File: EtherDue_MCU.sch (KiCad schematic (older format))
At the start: 30 parts, among them IC201 ATSAM3X8E, SW201 ERASE, SW202 RESET, U202 FDN340P, U203 LMV358IDGKR, X201 TXC 7A 12MHz 18pF, X202 ABS07L 32.768kHz

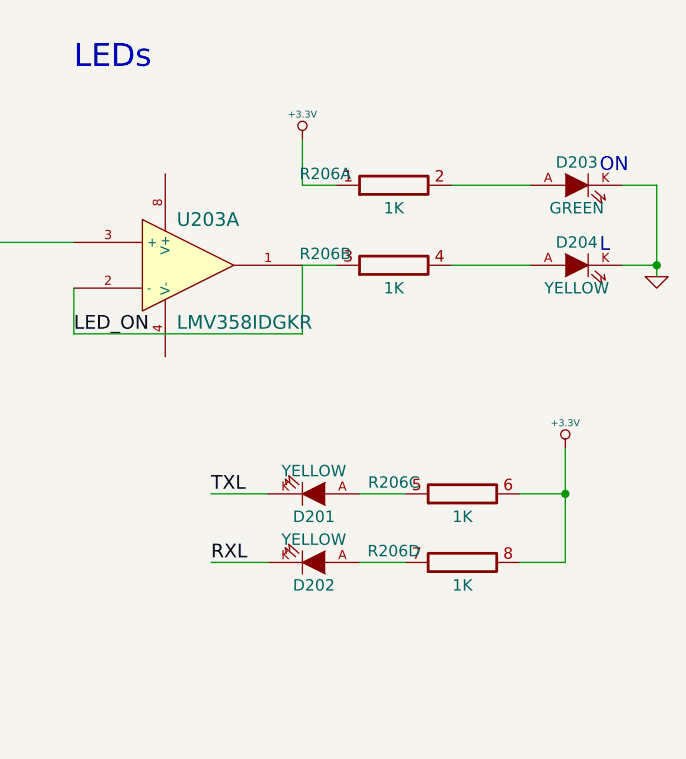
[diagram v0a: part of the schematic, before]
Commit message: Pre-autorouter hand routed traces
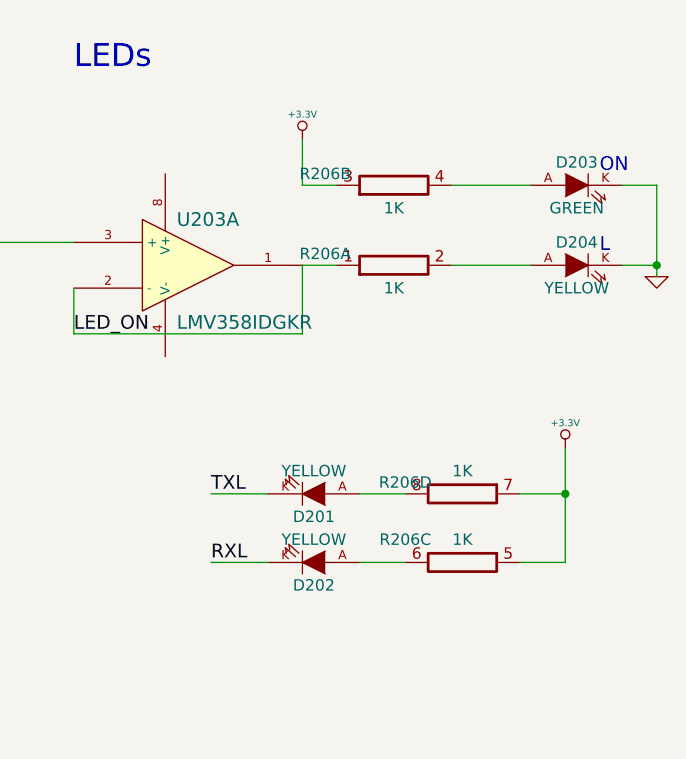
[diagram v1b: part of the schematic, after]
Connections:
- net +3.3V: now also R206.3 (7), R206.5 (7), R206.7; no longer R206.1 (7), R206.6 (8), R206.8
- net LED_ON: now also R206.1 (7); no longer R206.3 (7)
- net at R206.2 (8): now also D204.A; no longer D203.A
- net at R206.4 (8): now also D203.A; no longer D204.A
- net at D202.A: now also R206.6 (8); no longer R206.7
- net at D201.A: now also R206.8; no longer R206.5 (7)
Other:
- moved on the sheet: R206A, R206B, R206C, R206D
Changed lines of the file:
@@
-EESchema Schematic File Version 2  date Thu 06 Jun 2013 17:31:40 EST
+EESchema Schematic File Version 2  date Wed 19 Jun 2013 10:44:48 EST
 LIBS:freetronics_kicad_sch_lib
 LIBS:power
@@
 Sheet 2 6
 Title ""
-Date "6 jun 2013"
+Date "19 jun 2013"
 Rev ""
 Comp ""
@@
 L RES_PACK4_IND R206
 U 3 1 515CBE59
+P 14450 6800
+F 0 "R206" H 14700 6700 50  0000 C CNN
+F 1 "1K" H 14450 6700 50  0000 C CNN
+F 2 "" H 14450 6800 60  0001 C CNN
+F 3 "" H 14450 6800 60  0001 C CNN
+	3    14450 6800
+	-1   0    0    1
+$EndComp
+$Comp
+L RES_PACK4_IND R206
+U 4 1 515CBE58
 P 14450 6500
-F 0 "R206" H 14150 6550 50  0000 C CNN
+F 0 "R206" H 14700 6450 50  0000 C CNN
 F 1 "1K" H 14450 6400 50  0000 C CNN
 F 2 "" H 14450 6500 60  0001 C CNN
 F 3 "" H 14450 6500 60  0001 C CNN
-	3    14450 6500
-	1    0    0    -1
-$EndComp
-$Comp
-L RES_PACK4_IND R206
-U 4 1 515CBE58
-P 14450 6800
-F 0 "R206" H 14150 6850 50  0000 C CNN
-F 1 "1K" H 14450 6700 50  0000 C CNN
-F 2 "" H 14450 6800 60  0001 C CNN
-F 3 "" H 14450 6800 60  0001 C CNN
-	4    14450 6800
-	1    0    0    -1
+	4    14450 6500
+	-1   0    0    1
 $EndComp
 Text Label 13350 6800 0    60   ~ 0
@@
 L RES_PACK4_IND R206
 U 2 1 515CBD03
+P 14150 5150
+F 0 "R206" H 13850 5200 50  0000 C CNN
+F 1 "1K" H 14150 5050 50  0000 C CNN
+F 2 "" H 14150 5150 60  0001 C CNN
+F 3 "" H 14150 5150 60  0001 C CNN
+	2    14150 5150
+	1    0    0    -1
+$EndComp
+Text Notes 15050 5450 0    60   ~ 0
+L
+Text Notes 15050 5100 0    60   ~ 0
+ON
+$Comp
+L RES_PACK4_IND R206
+U 1 1 515CBD02
 P 14150 5500
 F 0 "R206" H 13850 5550 50  0000 C CNN
@@
 F 2 "" H 14150 5500 60  0001 C CNN
 F 3 "" H 14150 5500 60  0001 C CNN
-	2    14150 5500
-	1    0    0    -1
-$EndComp
-Text Notes 15050 5450 0    60   ~ 0
-L
-Text Notes 15050 5100 0    60   ~ 0
-ON
-$Comp
-L RES_PACK4_IND R206
-U 1 1 515CBD02
-P 14150 5150
-F 0 "R206" H 13850 5200 50  0000 C CNN
-F 1 "1K" H 14150 5050 50  0000 C CNN
-F 2 "" H 14150 5150 60  0001 C CNN
-F 3 "" H 14150 5150 60  0001 C CNN
-	1    14150 5150
-	1    0    0    -1
-$EndComp
+	1    14150 5500
+	1    0    0    -1
+$EndComp

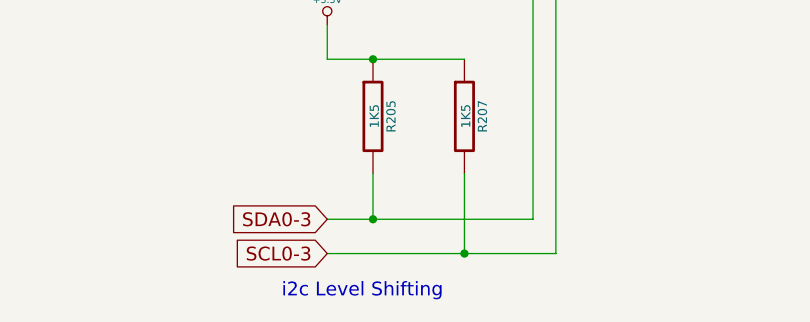
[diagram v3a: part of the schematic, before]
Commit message: Add 24AA025E48 EEPROM w/ unique MAC address
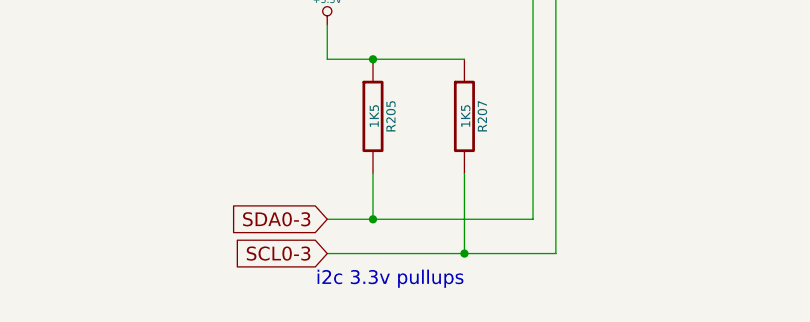
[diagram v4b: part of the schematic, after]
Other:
- note added: "i2c 3.3v pullups"
- note removed: "i2c Level Shifting"
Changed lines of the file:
@@
-EESchema Schematic File Version 2  date Fri 28 Jun 2013 16:34:50 EST
+EESchema Schematic File Version 2  date Thu 04 Jul 2013 10:55:52 EST
 LIBS:freetronics_kicad_sch_lib
 LIBS:power
@@
 $Descr A3 16535 11693
 encoding utf-8
-Sheet 2 6
+Sheet 2 7
 Title ""
-Date "27 jun 2013"
+Date "4 jul 2013"
 Rev ""
 Comp ""
@@
 Wire Wire Line
 	7600 10600 7600 8450
-Text Notes 6500 10950 0    60   ~ 0
-i2c Level Shifting
+Text Notes 6650 10900 0    60   ~ 0
+i2c 3.3v pullups
 NoConn ~ 7300 8450
 NoConn ~ 7200 8450

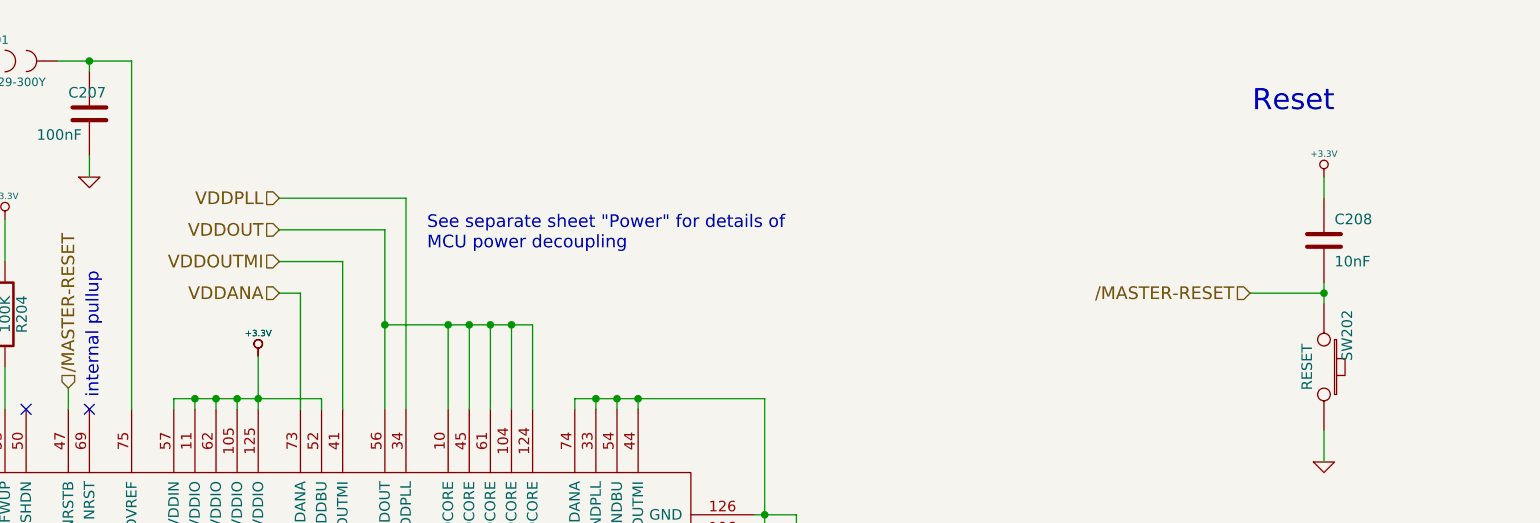
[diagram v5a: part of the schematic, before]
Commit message: Big power fixes: Fix major problem with VDDOUT/1.8V net, rearrange decoupling capacitors
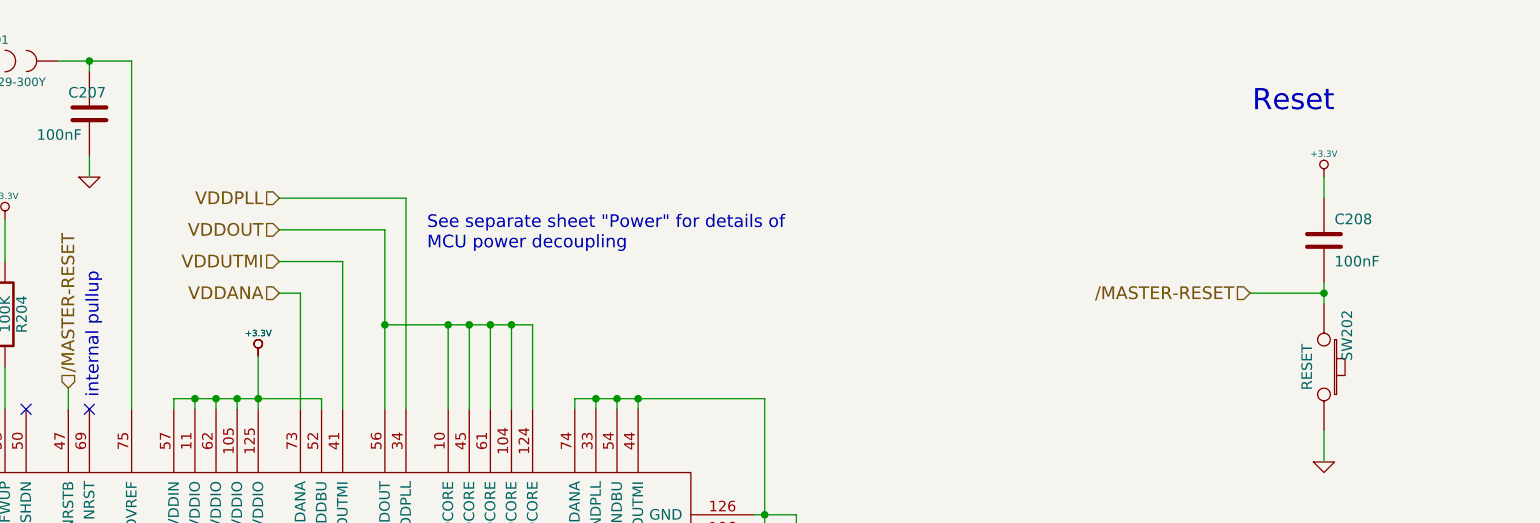
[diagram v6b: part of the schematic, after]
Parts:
- C208: value 10nF -> 100nF
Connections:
- net VDDOUTMI renamed VDDUTMI
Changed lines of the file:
@@
 P 13000 1950
 F 0 "C208" H 13050 2050 50  0000 L CNN
-F 1 "10nF" H 13050 1850 50  0000 L CNN
+F 1 "100nF" H 13050 1850 50  0000 L CNN
 F 2 "" H 13000 1950 60  0001 C CNN
 F 3 "" H 13000 1950 60  0001 C CNN
@@
 VDDANA
 Text HLabel 8050 2050 0    60   Input ~ 0
-VDDOUTMI
+VDDUTMI
 Text GLabel 12400 5400 0    60   Input ~ 0
 PWM13

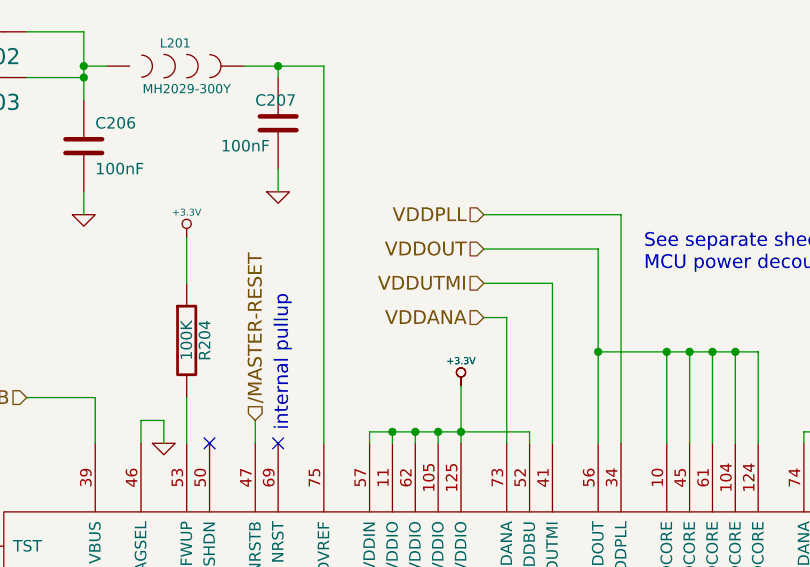
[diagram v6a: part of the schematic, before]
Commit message: Fix footprint association on resistor network for RJ45 connection
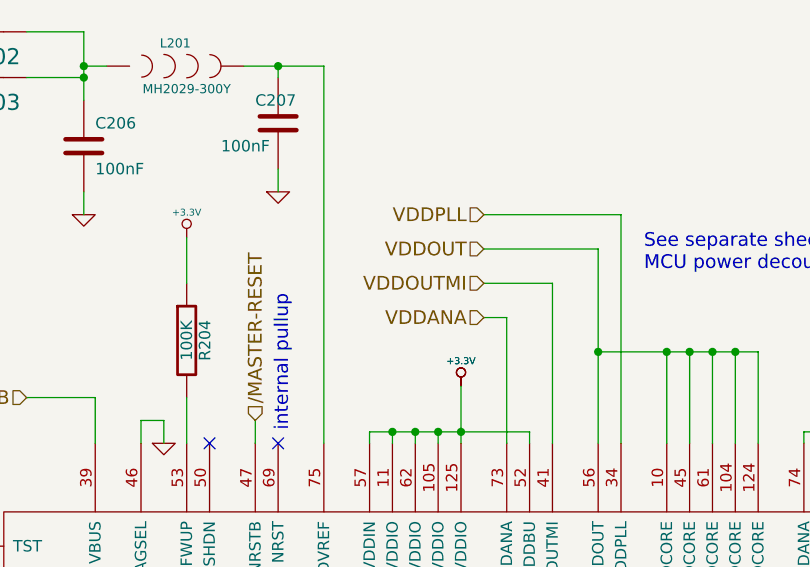
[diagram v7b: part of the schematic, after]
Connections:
- net VDDUTMI renamed VDDOUTMI
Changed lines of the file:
@@
 LIBS:valves
 LIBS:EtherDue-cache
-EELAYER 24 0
+EELAYER 27 0
 EELAYER END
 $Descr A3 16535 11693
@@
 Sheet 2 7
 Title ""
-Date "4 jul 2013"
+Date "20 nov 2013"
 Rev ""
 Comp ""
@@
 VDDANA
 Text HLabel 8050 2050 0    60   Input ~ 0
-VDDUTMI
+VDDOUTMI
 Text GLabel 12400 5400 0    60   Input ~ 0
 PWM13
